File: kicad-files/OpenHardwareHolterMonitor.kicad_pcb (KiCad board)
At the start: 6 copper layers, 131 x 80 mm, 151 parts, among them CON1 Micro_SD_Card, J1 Conn_02x06_Odd_Even, J10 Conn_01x01, J11 Conn_01x01, J12 USB_OTG, J13 USB_C_Receptacle, J2 Conn_01x01, J3 Conn_01x01, J4 Conn_01x01, J5 Conn_01x01, J6 Conn_01x01, J7 Conn_01x01, J8 Conn_01x01, J9 Conn_01x01, P1 Custom_FTDI, Q1 S8050, Q10 Q_PMOS_DGS, Q2 S8050, Q3 Q_NMOS_DGS, Q4 Q_NMOS_DGS, Q5 Q_NMOS_DGS, Q6 Q_NMOS_DGS, Q7 Q_PMOS_DGS, Q8 Q_PMOS_DGS, Q9 Q_PMOS_DGS, SW1 SW_SPDT, U1 ESP-WROOM-32, U2 ADS1298, U3 MCP73833, U4 MCP73833, U5 TPS2113A, U6 LP5912, U7 REM_3-xxxxS, Y1 32768Hz

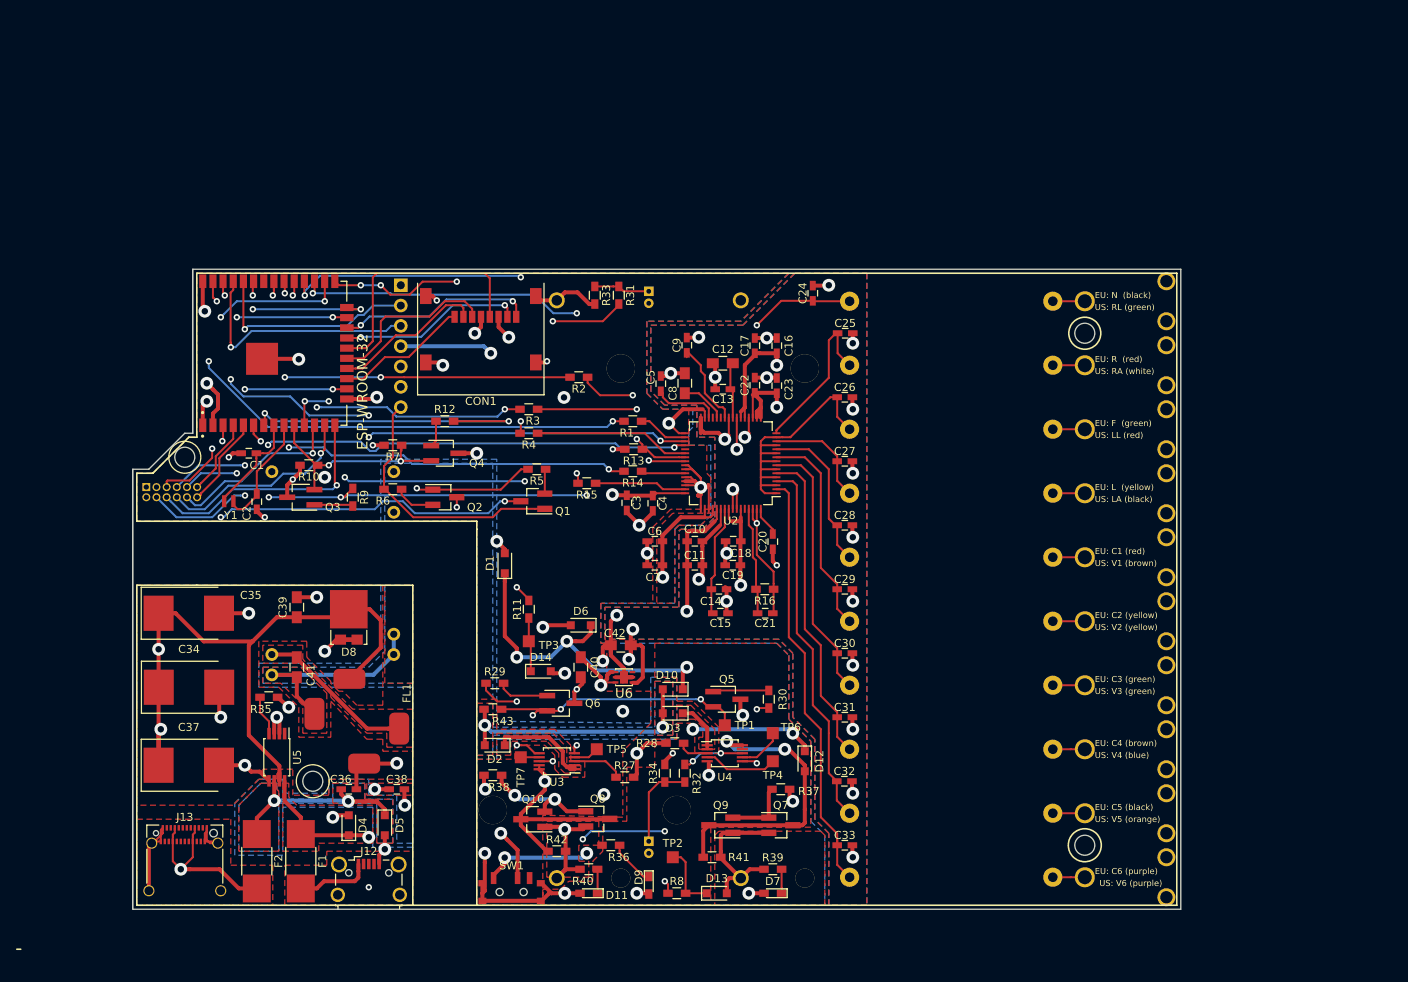
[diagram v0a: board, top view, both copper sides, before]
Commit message: add basic courtyards to footprints
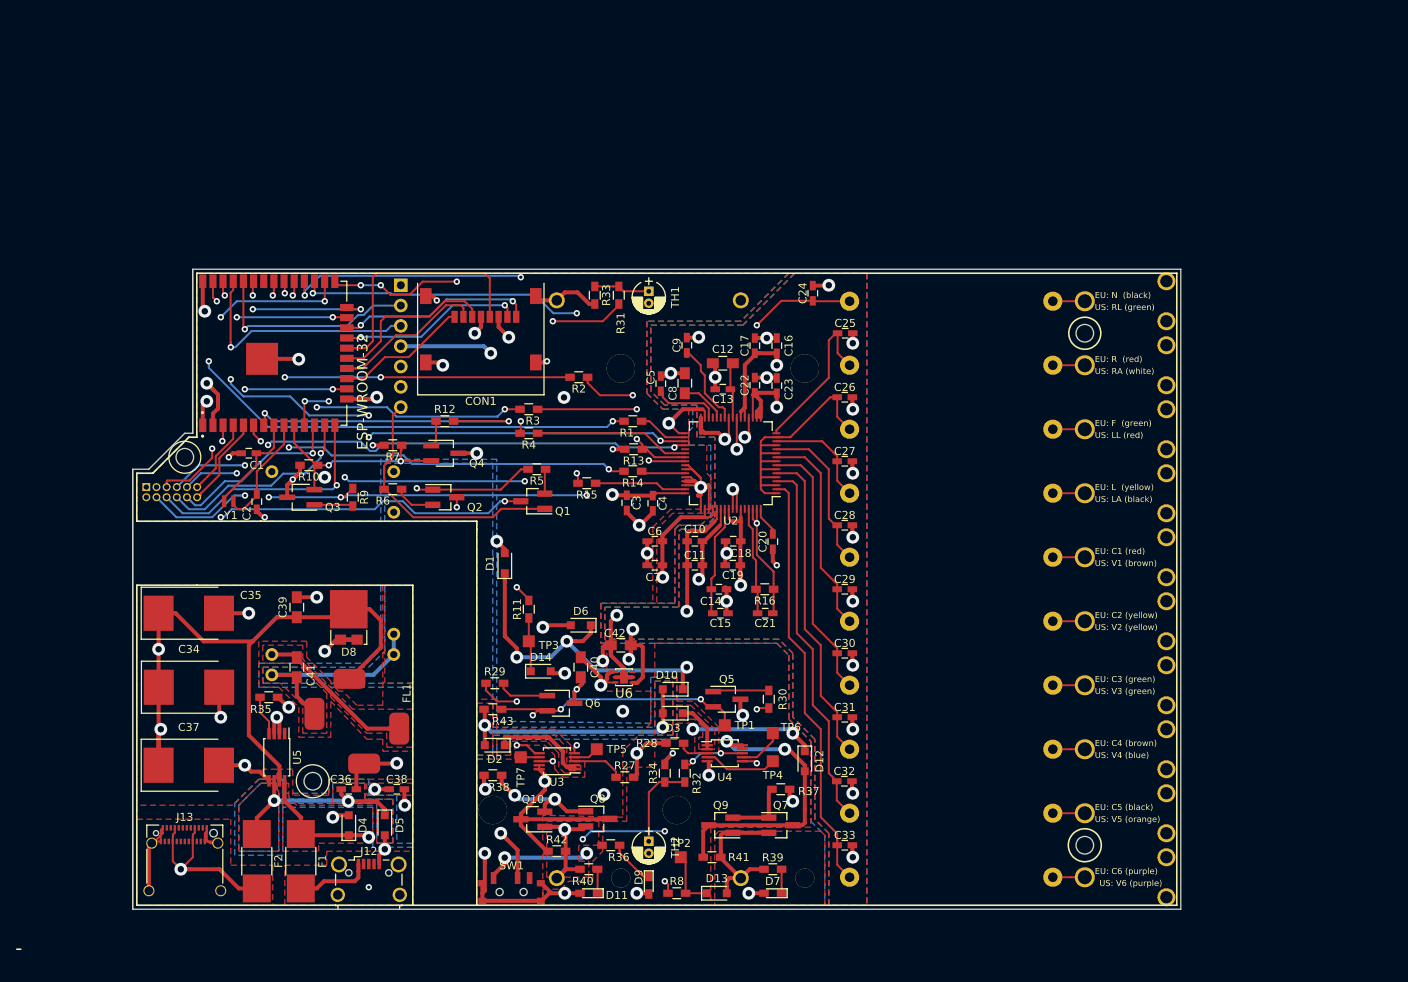
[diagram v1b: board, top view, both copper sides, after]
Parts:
- TH1, TH2: moved to F.Cu
- moved TP2 1.00 mm to (207.5, 93.5)
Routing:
- net /Vbat1: track 8.40 -> 7.40 mm

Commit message: add debug labels
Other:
- board text added: "IN1P"
- board text added: "IN1_8N"
- board text added: "IN2P"
- board text added: "IN3P"
- board text added: "IN4P"
- board text added: "IN5P"
- board text added: "IN6P"
- board text added: "IN7P"
- board text added: "IN8P"
- board text added: "RLDOUT"
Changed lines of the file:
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@@
     (pad 1 np_thru_hole circle (at 0 0) (size 2.2 2.2) (drill 2.2) (layers *.Cu *.Mask))
+  )
+  (gr_text IN8P (at 251.25 96) (layer F.SilkS)
+    (effects (font (size 0.762 0.762) (thickness 0.15)) (justify right))
+  )
+  (gr_text IN7P (at 251.25 88) (layer F.SilkS)
+    (effects (font (size 0.762 0.762) (thickness 0.15)) (justify right))
+  )
+  (gr_text IN6P (at 251.25 80) (layer F.SilkS)
+    (effects (font (size 0.762 0.762) (thickness 0.15)) (justify right))
+  )
+  (gr_text IN5P (at 251.25 72) (layer F.SilkS)
+    (effects (font (size 0.762 0.762) (thickness 0.15)) (justify right))
+  )
+  (gr_text IN4P (at 251.25 64) (layer F.SilkS)
+    (effects (font (size 0.762 0.762) (thickness 0.15)) (justify right))
+  )
+  (gr_text IN3P (at 251.25 56.25) (layer F.SilkS)
+    (effects (font (size 0.762 0.762) (thickness 0.15)) (justify right))
+  )
+  (gr_text IN2P (at 251.25 48) (layer F.SilkS)
+    (effects (font (size 0.762 0.762) (thickness 0.15)) (justify right))
+  )
+  (gr_text IN1_8N (at 251.46 40) (layer F.SilkS)
+    (effects (font (size 0.762 0.762) (thickness 0.15)) (justify right))
+  )
+  (gr_text IN1P (at 250 32) (layer F.SilkS)
+    (effects (font (size 0.762 0.762) (thickness 0.15)))
+  )
+  (gr_text RLDOUT (at 251.25 24.25) (layer F.SilkS)
+    (effects (font (size 0.762 0.762) (thickness 0.15)) (justify right))
   )
   (gr_text "US: V6 (purple)" (at 263.75 96.75) (layer F.SilkS)

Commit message: align physical items with schematic
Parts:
- MH_NE1: renamed from MH_NE; value MountingHole_2.2mm_M2_ISO7380 -> Mounting_Hole
- MH_NW1: renamed from MH_NW; value MountingHole_2.2mm_M2_ISO7380 -> Mounting_Hole
- MH_SE1: renamed from MH_SE; value MountingHole_2.2mm_M2_ISO7380 -> Mounting_Hole
- MH_SW1: renamed from MH_SW; value MountingHole_2.2mm_M2_ISO7380 -> Mounting_Hole
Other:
- board text added: "TODO Fiducial marks"
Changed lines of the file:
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@@
   (general
     (thickness 1.6)
-    (drawings 49)
+    (drawings 60)
     (tracks 1394)
     (zones 0)
@@
     (add_net "Net-(Q7-Pad1)")
   )
+  (module Alps:ALPS_SSSS810701 (layer F.Cu)
+    (at 186.35 97.85)
+    (fp_text reference SW1 (at 0 -3.3) (layer F.SilkS)
+      (effects (font (size 1 1) (thickness 0.15)))
+    )
+    (fp_text value SW_SPDT (at 0 -0.5) (layer F.Fab)
+      (effects (font (size 1 1) (thickness 0.15)))
+    )
+    (fp_line (start -4.2 -2.6) (end 4.2 -2.6) (layer F.CrtYd) (width 0.15))
+    (fp_line (start -4.2 -2.6) (end -4.2 1.6) (layer F.CrtYd) (width 0.15))
+    (fp_line (start -4.2 1.6) (end 4.2 1.6) (layer F.CrtYd) (width 0.15))
+    (fp_line (start 4.2 1.6) (end 4.2 -2.6) (layer F.CrtYd) (width 0.15))
+    (pad "" np_thru_hole circle (at -1.5 0) (size 0.9 0.9) (drill 0.9) (layers *.Cu *.Mask))
+    (pad "" np_thru_hole circle (at 1.5 0) (size 0.9 0.9) (drill 0.9) (layers *.Cu *.Mask))
+    (pad 2 smd rect (at 0.75 -1.75) (size 0.7 1.5) (layers F.Cu F.Paste F.Mask)
+      (net 32 /power/REGULATOR_IN))
+    (pad 1 smd rect (at -2.25 -1.75) (size 0.7 1.5) (layers F.Cu F.Paste F.Mask)
+      (net 28 "Net-(C40-Pad1)"))
+    (pad 3 smd rect (at 2.25 -1.75) (size 0.7 1.5) (layers F.Cu F.Paste F.Mask)
+      (net 109 "Net-(SW1-Pad3)"))
+    (pad SHIELD smd rect (at -3.65 -1.1) (size 1 0.8) (layers F.Cu F.Paste F.Mask)
+      (net 1 GND))
+    (pad SHIELD smd rect (at -3.65 1.1) (size 1 0.8) (layers F.Cu F.Paste F.Mask)
+      (net 1 GND))
+    (pad SHIELD smd rect (at 3.65 -1.1) (size 1 0.8) (layers F.Cu F.Paste F.Mask)
+      (net 1 GND))
+    (pad SHIELD smd rect (at 3.65 1.1) (size 1 0.8) (layers F.Cu F.Paste F.Mask)
+      (net 1 GND))
+  )
   (module crystals:K161 (layer F.Cu)
     (at 151 49)
@@
     (fp_line (start 39 11) (end 39 -11) (layer B.CrtYd) (width 0.15))
     (fp_line (start -39 11) (end 39 11) (layer B.CrtYd) (width 0.15))
-    (fp_text user - (at -41 0 270) (layer B.SilkS)
+    (fp_text user - (at -31.75 0 270) (layer B.SilkS)
       (effects (font (size 3 3) (thickness 0.15)) (justify mirror))
     )
-    (fp_text user + (at 41 0 270) (layer B.SilkS)
+    (fp_text user + (at 33 0 270) (layer B.SilkS)
       (effects (font (size 3 3) (thickness 0.15)) (justify mirror))
     )
@@
     (fp_line (start 39 11) (end 39 -11) (layer B.CrtYd) (width 0.15))
     (fp_line (start -39 11) (end 39 11) (layer B.CrtYd) (width 0.15))
-    (fp_text user - (at -41 0 270) (layer B.SilkS)
+    (fp_text user - (at -31.5 0 270) (layer B.SilkS)
       (effects (font (size 3 3) (thickness 0.15)) (justify mirror))
     )
-    (fp_text user + (at 41 0 270) (layer B.SilkS)
+    (fp_text user + (at 33.25 -0.25 270) (layer B.SilkS)
       (effects (font (size 3 3) (thickness 0.15)) (justify mirror))
     )
@@
     (tags "mounting hole 2.2mm no annular m2 iso7380")
     (attr virtual)
-    (fp_text reference MH_SE (at 0 -2.75) (layer F.SilkS) hide
+    (fp_text reference MH_SE1 (at 0 -2.75) (layer F.SilkS) hide
       (effects (font (size 1 1) (thickness 0.15)))
     )
-    (fp_text value MountingHole_2.2mm_M2_ISO7380 (at 0 2.75) (layer F.Fab)
+    (fp_text value Mounting_Hole (at 0 2.75) (layer F.Fab)
       (effects (font (size 1 1) (thickness 0.15)))
     )
@@
     (tags "mounting hole 2.2mm no annular m2 iso7380")
     (attr virtual)
-    (fp_text reference MH_NE (at 0 -2.75) (layer F.SilkS) hide
+    (fp_text reference MH_NE1 (at 0 -2.75) (layer F.SilkS) hide
       (effects (font (size 1 1) (thickness 0.15)))
     )
-    (fp_text value MountingHole_2.2mm_M2_ISO7380 (at 0 2.75) (layer F.Fab)
+    (fp_text value Mounting_Hole (at 0 2.75) (layer F.Fab)
       (effects (font (size 1 1) (thickness 0.15)))
     )
@@
     (tags "mounting hole 2.2mm no annular m2 iso7380")
     (attr virtual)
-    (fp_text reference MH_NW (at 0 -2.75) (layer F.SilkS) hide
+    (fp_text reference MH_NW1 (at 0 -2.75) (layer F.SilkS) hide
       (effects (font (size 1 1) (thickness 0.15)))
     )
-    (fp_text value MountingHole_2.2mm_M2_ISO7380 (at 0 2.75) (layer F.Fab)
+    (fp_text value Mounting_Hole (at 0 2.75) (layer F.Fab)
       (effects (font (size 1 1) (thickness 0.15)))
     )
@@
       (net 30 "Net-(C41-Pad1)"))
   )
-  (module Alps:ALPS_SSSS810701 (layer F.Cu)
-    (at 186.35 97.85)
-    (fp_text reference SW1 (at 0 -3.3) (layer F.SilkS)
-      (effects (font (size 1 1) (thickness 0.15)))
-    )
-    (fp_text value SW_SPDT (at 0 -0.5) (layer F.Fab)
-      (effects (font (size 1 1) (thickness 0.15)))
-    )
-    (fp_line (start 4.2 1.6) (end 4.2 -2.6) (layer F.CrtYd) (width 0.15))
-    (fp_line (start -4.2 1.6) (end 4.2 1.6) (layer F.CrtYd) (width 0.15))
-    (fp_line (start -4.2 -2.6) (end -4.2 1.6) (layer F.CrtYd) (width 0.15))
-    (fp_line (start -4.2 -2.6) (end 4.2 -2.6) (layer F.CrtYd) (width 0.15))
-    (pad GND smd rect (at 3.65 1.1) (size 1 0.8) (layers F.Cu F.Paste F.Mask)
-      (net 1 GND))
-    (pad GND smd rect (at 3.65 -1.1) (size 1 0.8) (layers F.Cu F.Paste F.Mask)
-      (net 1 GND))
-    (pad GND smd rect (at -3.65 1.1) (size 1 0.8) (layers F.Cu F.Paste F.Mask)
-      (net 1 GND))
-    (pad GND smd rect (at -3.65 -1.1) (size 1 0.8) (layers F.Cu F.Paste F.Mask)
-      (net 1 GND))
-    (pad 3 smd rect (at 2.25 -1.75) (size 0.7 1.5) (layers F.Cu F.Paste F.Mask)
-      (net 109 "Net-(SW1-Pad3)"))
-    (pad 1 smd rect (at -2.25 -1.75) (size 0.7 1.5) (layers F.Cu F.Paste F.Mask)
-      (net 28 "Net-(C40-Pad1)"))
-    (pad 2 smd rect (at 0.75 -1.75) (size 0.7 1.5) (layers F.Cu F.Paste F.Mask)
-      (net 32 /power/REGULATOR_IN))
-    (pad "" np_thru_hole circle (at 1.5 0) (size 0.9 0.9) (drill 0.9) (layers *.Cu *.Mask))
-    (pad "" np_thru_hole circle (at -1.5 0) (size 0.9 0.9) (drill 0.9) (layers *.Cu *.Mask))
-  )
   (module Measurement_Points:Measurement_Point_Square-SMD-Pad_Small (layer F.Cu)
     (at 188.5 66.5 180)
@@
     (tags "mounting hole 2.2mm no annular m2 iso7380")
     (attr virtual)
-    (fp_text reference MH_SW (at 0 -2.75) (layer F.SilkS) hide
+    (fp_text reference MH_SW1 (at 0 -2.75) (layer F.SilkS) hide
       (effects (font (size 1 1) (thickness 0.15)))
     )
-    (fp_text value MountingHole_2.2mm_M2_ISO7380 (at 0 2.75) (layer F.Fab)
+    (fp_text value Mounting_Hole (at 0 2.75) (layer F.Fab)
       (effects (font (size 1 1) (thickness 0.15)))
     )
@@
     (pad 1 np_thru_hole circle (at 0 0) (size 2.2 2.2) (drill 2.2) (layers *.Cu *.Mask))
   )
+  (gr_text "TODO Fiducial marks" (at 204.25 105.5) (layer F.SilkS)
+    (effects (font (size 1.5 1.5) (thickness 0.3)))
+  )
   (gr_text IN8P (at 251.25 96) (layer F.SilkS)

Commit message: add fiducial marks
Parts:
- added ?: Fiducial_1mm_Dia_2.54mm_Outer_CopperTop, Fiducial:Fiducial_1mm_Dia_2.54mm_Outer_CopperTop, F.Cu at (198.5, 55.0)
- added ?: Fiducial_1mm_Dia_2.54mm_Outer_CopperTop, Fiducial:Fiducial_1mm_Dia_2.54mm_Outer_CopperTop, F.Cu at (264.5, 92.0)
- added ?: Fiducial_1mm_Dia_2.54mm_Outer_CopperTop, Fiducial:Fiducial_1mm_Dia_2.54mm_Outer_CopperTop, F.Cu at (142.5, 87.0)
- added ?: Fiducial_1mm_Dia_2.54mm_Outer_CopperTop, Fiducial:Fiducial_1mm_Dia_2.54mm_Outer_CopperTop, F.Cu at (264.5, 27.5)
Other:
- board text removed: "TODO Fiducial marks"
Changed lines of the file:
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@@
-(kicad_pcb (version 20171130) (host pcbnew 5.0.1+dfsg1-3)
+(kicad_pcb (version 20171130) (host pcbnew 5.0.2-bee76a0~70~ubuntu18.04.1)
   (general
     (thickness 1.6)
-    (drawings 60)
+    (drawings 59)
     (tracks 1394)
     (zones 0)
-    (modules 151)
+    (modules 155)
     (nets 144)
   )
@@
     (add_net "Net-(Q7-Pad1)")
   )
+  (module Fiducial:Fiducial_1mm_Dia_2.54mm_Outer_CopperTop (layer F.Cu)
+    (at 198.5 55)
+    (descr "Circular Fiducial, 1mm bare copper top, 2.54mm keepout")
+    (tags fiducial)
+    (attr smd)
+    (fp_text reference "" (at 0 -2.5) (layer F.SilkS)
+      (effects (font (size 1 1) (thickness 0.15)))
+    )
+    (fp_text value Fiducial_1mm_Dia_2.54mm_Outer_CopperTop (at 0 2.5) (layer F.Fab)
+      (effects (font (size 1 1) (thickness 0.15)))
+    )
+    (fp_circle (center 0 0) (end 1.55 0) (layer F.CrtYd) (width 0.05))
+    (fp_text user %R (at 0 0) (layer F.Fab)
+      (effects (font (size 1 1) (thickness 0.15)))
+    )
+    (pad "" smd circle (at 0 0) (size 1 1) (layers F.Cu F.Mask)
+      (solder_mask_margin 0.77) (clearance 0.77))
+  )
+  (module Fiducial:Fiducial_1mm_Dia_2.54mm_Outer_CopperTop (layer F.Cu)
+    (at 264.5 92)
+    (descr "Circular Fiducial, 1mm bare copper top, 2.54mm keepout")
+    (tags fiducial)
+    (attr smd)
+    (fp_text reference "" (at 0.5 0) (layer F.SilkS) hide
+      (effects (font (size 1 1) (thickness 0.15)))
+    )
+    (fp_text value Fiducial_1mm_Dia_2.54mm_Outer_CopperTop (at 0 2.5) (layer F.Fab)
+      (effects (font (size 1 1) (thickness 0.15)))
+    )
+    (fp_circle (center 0 0) (end 1.55 0) (layer F.CrtYd) (width 0.05))
+    (fp_text user %R (at 0 0) (layer F.Fab)
+      (effects (font (size 1 1) (thickness 0.15)))
+    )
+    (pad "" smd circle (at 0 0) (size 1 1) (layers F.Cu F.Mask)
+      (solder_mask_margin 0.77) (clearance 0.77))
+  )
   (module Alps:ALPS_SSSS810701 (layer F.Cu)
     (at 186.35 97.85)
@@
     (pad 1 np_thru_hole circle (at 0 0) (size 2.2 2.2) (drill 2.2) (layers *.Cu *.Mask))
   )
-  (gr_text "TODO Fiducial marks" (at 204.25 105.5) (layer F.SilkS)
-    (effects (font (size 1.5 1.5) (thickness 0.3)))
+  (module Fiducial:Fiducial_1mm_Dia_2.54mm_Outer_CopperTop (layer F.Cu)
+    (at 142.5 87)
+    (descr "Circular Fiducial, 1mm bare copper top, 2.54mm keepout")
+    (tags fiducial)
+    (attr smd)
+    (fp_text reference "" (at 3.5 0) (layer F.SilkS) hide
+      (effects (font (size 1 1) (thickness 0.15)))
+    )
+    (fp_text value Fiducial_1mm_Dia_2.54mm_Outer_CopperTop (at 0 2.5) (layer F.Fab)
+      (effects (font (size 1 1) (thickness 0.15)))
+    )
+    (fp_text user %R (at 0 0) (layer F.Fab)
+      (effects (font (size 1 1) (thickness 0.15)))
+    )
+    (fp_circle (center 0 0) (end 1.55 0) (layer F.CrtYd) (width 0.05))
+    (pad "" smd circle (at 0 0) (size 1 1) (layers F.Cu F.Mask)
+      (solder_mask_margin 0.77) (clearance 0.77))
+  )
+  (module Fiducial:Fiducial_1mm_Dia_2.54mm_Outer_CopperTop (layer F.Cu)
+    (at 264.5 27.5)
+    (descr "Circular Fiducial, 1mm bare copper top, 2.54mm keepout")
+    (tags fiducial)
+    (attr smd)
+    (fp_text reference "" (at 0.5 0) (layer F.SilkS) hide
+      (effects (font (size 1 1) (thickness 0.15)))
+    )
+    (fp_text value Fiducial_1mm_Dia_2.54mm_Outer_CopperTop (at 0 2.5) (layer F.Fab)
+      (effects (font (size 1 1) (thickness 0.15)))
+    )
+    (fp_circle (center 0 0) (end 1.55 0) (layer F.CrtYd) (width 0.05))
+    (fp_text user %R (at 0 0) (layer F.Fab)
+      (effects (font (size 1 1) (thickness 0.15)))
+    )
+    (pad "" smd circle (at 0 0) (size 1 1) (layers F.Cu F.Mask)
+      (solder_mask_margin 0.77) (clearance 0.77))
   )
   (gr_text IN8P (at 251.25 96) (layer F.SilkS)
